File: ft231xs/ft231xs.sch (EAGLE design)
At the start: 23 parts, among them U3 AP2112K-3.3V

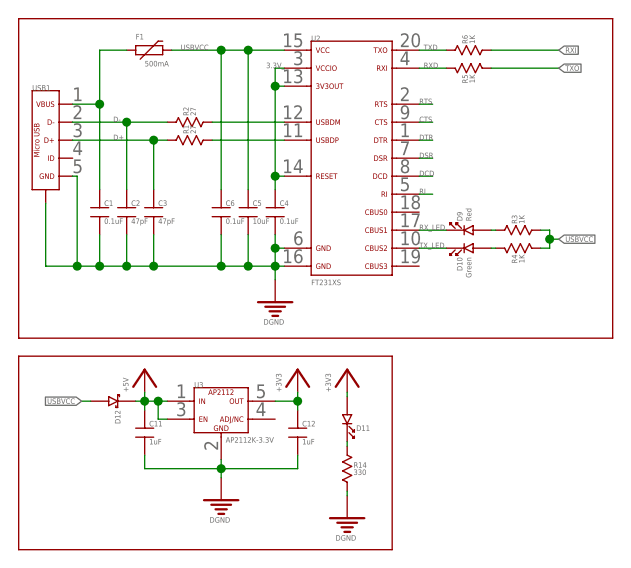
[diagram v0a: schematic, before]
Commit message: add 232 module and finish the ft231
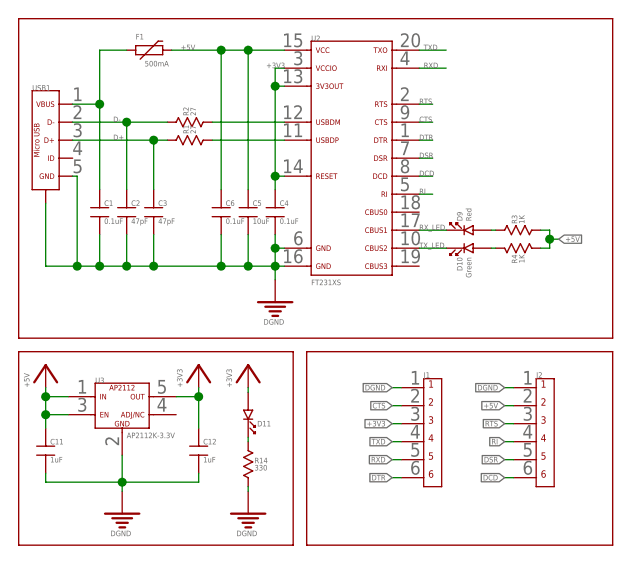
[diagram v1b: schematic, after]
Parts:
- removed D12: (no value), Diodes:SCHOTTKY_DIODE_0805
- removed R5, R6: 1K, Resistors:RESISTOR_0805
- added J1, J2: (no value), Connectors:6PIN_HEADER_PITCH2.54MM_TH
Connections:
- removed net 3.3V_: C4.1, U2.13, U2.14, U2.3
- removed net RXI: R6.2
- removed net TXO: R5.2
- removed net USBVCC: C5.1, C6.1, D12.2, F1.2, R3.2, R4.2, U2.15
- net +3V3: now also C4.1, J1.3, U2.13, U2.14, U2.3
- net +5V: now also C5.1, C6.1, F1.2, J2.2, R3.2, R4.2, U2.15; no longer D12.1
- net CTS: now also J1.2
- net DCD: now also J2.6
- net DGND: now also J1.1, J2.1
- net DSR: now also J2.5
- net DTR: now also J1.6
- net RI: now also J2.4
- net RTS: now also J2.3
- net RXD: now also J1.5; no longer R5.1
- net TXD: now also J1.4; no longer R6.1
- net VBUS: now also USB1.VBUS
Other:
- moved on the sheet: C11, C12, D11, R14, U3

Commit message: the ft231xs is ready
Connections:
- net +3V3: now also D11.A; no longer D11.2
- net N$32: now also D9.A; no longer D9.2
- net N$33: now also D10.A; no longer D10.2
- net N$35: now also D11.K; no longer D11.1
- net RX_LED: now also D9.K; no longer D9.1
- net TX_LED: now also D10.K; no longer D10.1
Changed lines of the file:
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@@
 <?xml version="1.0" encoding="utf-8"?>
 <!DOCTYPE eagle SYSTEM "eagle.dtd">
-<eagle version="7.5.0">
+<eagle version="8.1.1">
 <drawing>
 <settings>
@@
 <setting verticaltext="up"/>
 </settings>
-<grid distance="0.5" unitdist="mm" unit="mm" style="lines" multiple="1" display="yes" altdistance="0.01" altunitdist="mm" altunit="mm"/>
+<grid distance="0.1" unitdist="inch" unit="inch" style="lines" multiple="1" display="no" altdistance="0.01" altunitdist="inch" altunit="inch"/>
 <layers>
 <layer number="1" name="Top" color="4" fill="1" visible="no" active="no"/>
 <layer number="2" name="Route2" color="1" fill="3" visible="no" active="no"/>
 <layer number="3" name="Route3" color="4" fill="3" visible="no" active="no"/>
+<layer number="4" name="Route4" color="1" fill="4" visible="no" active="no"/>
+<layer number="5" name="Route5" color="4" fill="4" visible="no" active="no"/>
+<layer number="6" name="Route6" color="1" fill="8" visible="no" active="no"/>
+<layer number="7" name="Route7" color="4" fill="8" visible="no" active="no"/>
+<layer number="8" name="Route8" color="1" fill="2" visible="no" active="no"/>
+<layer number="9" name="Route9" color="4" fill="2" visible="no" active="no"/>
+<layer number="10" name="Route10" color="1" fill="7" visible="no" active="no"/>
+<layer number="11" name="Route11" color="4" fill="7" visible="no" active="no"/>
+<layer number="12" name="Route12" color="1" fill="5" visible="no" active="no"/>
+<layer number="13" name="Route13" color="4" fill="5" visible="no" active="no"/>
 <layer number="14" name="Route14" color="1" fill="6" visible="no" active="no"/>
 <layer number="15" name="Route15" color="4" fill="6" visible="no" active="no"/>
@@
 <junction x="22.5" y="31.5"/>
 <pinref part="USB1" gate="G$1" pin="GND"/>
-<wire x1="5.96" y1="41.5" x2="6.5" y2="41.5" width="0.1524" layer="91"/>
+<wire x1="6" y1="41.5" x2="6.5" y2="41.5" width="0.1524" layer="91"/>
 <wire x1="6.5" y1="41.5" x2="6.5" y2="31.5" width="0.1524" layer="91"/>
 <junction x="6.5" y="31.5"/>
@@
 <segment>
 <pinref part="USB1" gate="G$1" pin="D+"/>
-<wire x1="5.96" y1="45.5" x2="15" y2="45.5" width="0.1524" layer="91"/>
+<wire x1="6" y1="45.5" x2="15" y2="45.5" width="0.1524" layer="91"/>
 <pinref part="R1" gate="G$1" pin="1"/>
 <pinref part="C3" gate="G$1" pin="1"/>
@@
 <segment>
 <pinref part="USB1" gate="G$1" pin="D-"/>
-<wire x1="5.96" y1="47.5" x2="12" y2="47.5" width="0.1524" layer="91"/>
+<wire x1="6" y1="47.5" x2="12" y2="47.5" width="0.1524" layer="91"/>
 <pinref part="R2" gate="G$1" pin="1"/>
 <pinref part="C2" gate="G$1" pin="1"/>
@@
 <junction x="9" y="49.5"/>
 <pinref part="USB1" gate="G$1" pin="VBUS"/>
-<wire x1="5.96" y1="49.5" x2="9" y2="49.5" width="0.1524" layer="91"/>
+<wire x1="6" y1="49.5" x2="9" y2="49.5" width="0.1524" layer="91"/>
 </segment>
 </net>
 <net name="RX_LED" class="0">
 <segment>
-<pinref part="D9" gate="G$1" pin="1"/>
+<pinref part="D9" gate="G$1" pin="K"/>
 <pinref part="U2" gate="G$1" pin="17"/>
 <wire x1="47.5" y1="35.5" x2="44.5" y2="35.5" width="0.1524" layer="91"/>
@@
 <net name="TX_LED" class="0">
 <segment>
-<pinref part="D10" gate="G$1" pin="1"/>
+<pinref part="D10" gate="G$1" pin="K"/>
 <pinref part="U2" gate="G$1" pin="10"/>
 <wire x1="47.5" y1="33.5" x2="44.5" y2="33.5" width="0.1524" layer="91"/>
@@
 <net name="N$32" class="0">
 <segment>
-<pinref part="D9" gate="G$1" pin="2"/>
+<pinref part="D9" gate="G$1" pin="A"/>
 <pinref part="R3" gate="G$1" pin="1"/>
 <wire x1="52.5" y1="35.5" x2="53" y2="35.5" width="0.1524" layer="91"/>
@@
 <net name="N$33" class="0">
 <segment>
-<pinref part="D10" gate="G$1" pin="2"/>
+<pinref part="D10" gate="G$1" pin="A"/>
 <pinref part="R4" gate="G$1" pin="1"/>
 <wire x1="52.5" y1="33.5" x2="53" y2="33.5" width="0.1524" layer="91"/>
@@
 </segment>
 <segment>
-<pinref part="D11" gate="G$1" pin="2"/>
+<pinref part="D11" gate="G$1" pin="A"/>
 <wire x1="25.5" y1="18" x2="25.5" y2="17.5" width="0.15" layer="91"/>
 <pinref part="+3V5" gate="G$1" pin="+3V3"/>
@@
 <net name="N$35" class="0">
 <segment>
-<pinref part="D11" gate="G$1" pin="1"/>
+<pinref part="D11" gate="G$1" pin="K"/>
 <pinref part="R14" gate="G$1" pin="1"/>
 <wire x1="25.5" y1="12.5" x2="25.5" y2="12" width="0.15" layer="91"/>
